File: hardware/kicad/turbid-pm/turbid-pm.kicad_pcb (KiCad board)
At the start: 2 copper layers, 10 parts, among them J1 Pi connection, J2 PMS 7003, J3 Turbidity

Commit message: added 3d print source
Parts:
- removed D2: Turbidity Ok LED, LED_THT:LED_D3.0mm_Clear
- added J4: Temp sensor A, Connector_PinSocket_2.54mm:PinSocket_1x03_P2.54mm_Vertical, F.Cu at (94.0, 81.3)
- added J5: Temp sensor B, Connector_PinSocket_2.54mm:PinSocket_1x03_P2.54mm_Vertical, F.Cu at (102.9, 81.3)
- added R5: 4.7K, Resistor_THT:R_Axial_DIN0207_L6.3mm_D2.5mm_P10.16mm_Horizontal, F.Cu at (100.3, 68.6)
- J1: value Pi connection -> Raspbery Pi
- J3: value Turbidity -> Turbidity sensor
- R1: value R -> 1K
- R2: value R -> 10K
- R4: value R -> 4.7K
- moved R4 5.24 mm to (97.8, 68.6), turned to 270 degrees
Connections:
- net /rx renamed /RX
- net /scl renamed /SCL
- net /sda renamed /SDA
- net /tx renamed /TX
- A1 pad 8: (no net) -> Net-(A1-Pad8)
- R4 pad 2: Net-(D2-Pad2) -> +5V
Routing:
- net +5V: track 77.3 -> 116.2 mm, vias 5 -> 8
- net Net-(A1-Pad7): track 10.2 -> 35.6 mm, vias 0 -> 3
- net Net-(A1-Pad8): track 0.00 -> 14.5 mm, vias 0 -> 2
- net Net-(D2-Pad2): track 12.7 -> 0.00 mm
- net Earth: track 180.3 -> 186.7 mm
- net Net-(A1-Pad5): track 33.6 -> 34.9 mm, vias 2 -> 3

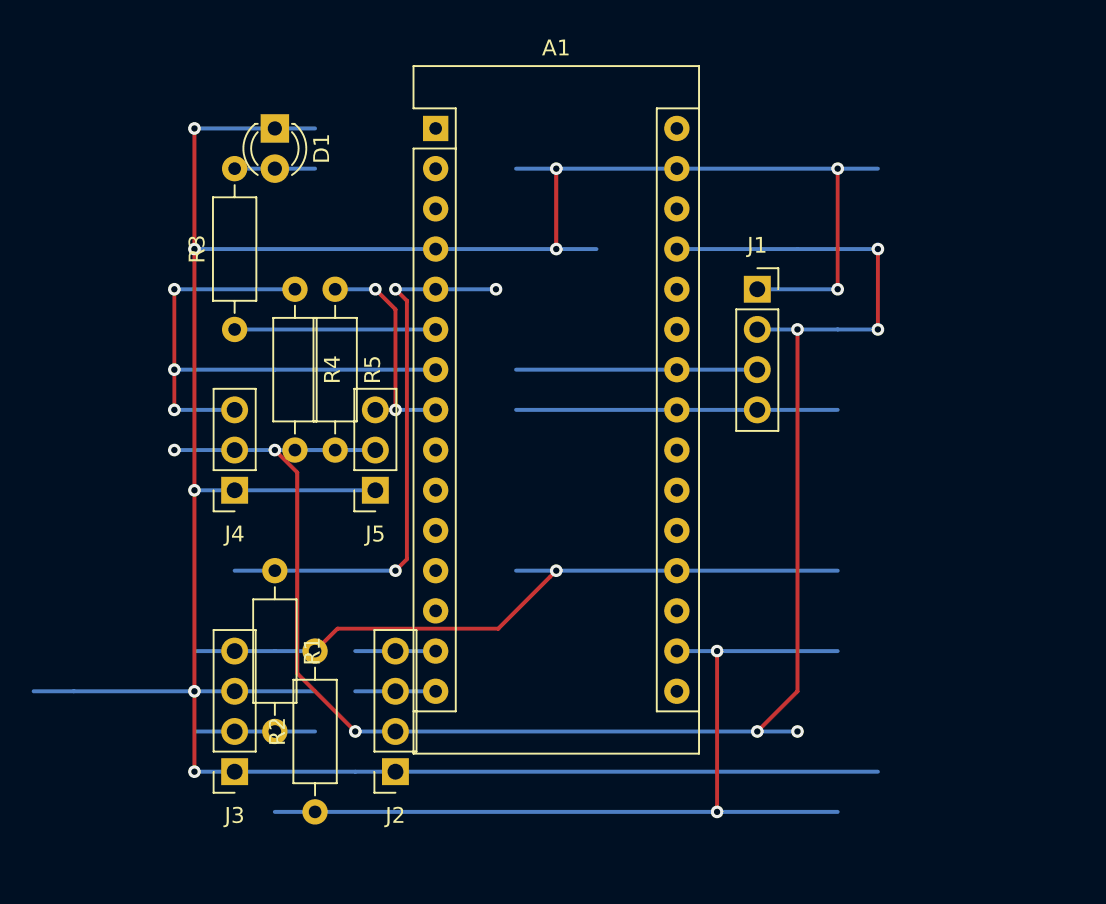
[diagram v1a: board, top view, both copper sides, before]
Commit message: new firmware and docs
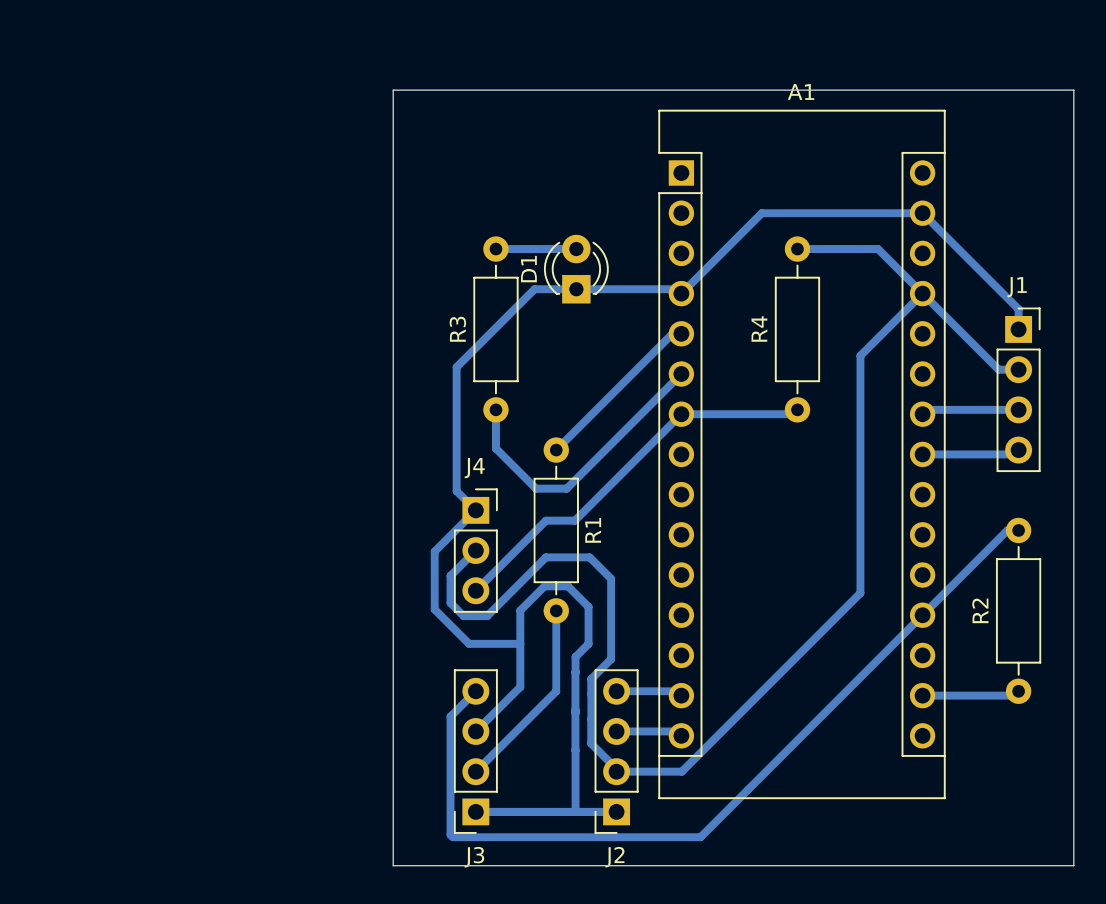
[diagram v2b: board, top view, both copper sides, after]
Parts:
- removed J5: Temp sensor B, Connector_PinSocket_2.54mm:PinSocket_1x03_P2.54mm_Vertical
- removed R5: 4.7K, Resistor_THT:R_Axial_DIN0207_L6.3mm_D2.5mm_P10.16mm_Horizontal
- J4: value Temp sensor A -> Temp sensor
- moved R2 45.1 mm to (143.5, 94.0)
- moved R4 32.7 mm to (129.5, 76.2), turned to 90 degrees
- moved D1 21.6 mm to (115.6, 68.6), turned to 90 degrees
- moved R1 19.3 mm to (114.3, 78.7)
- moved R3 17.3 mm to (110.5, 76.2)
- moved J1 16.7 mm to (143.5, 71.1)
- moved A1 15.8 mm to (122.2, 61.2)
- moved J3 15.5 mm to (109.2, 101.6)
- moved J4 15.3 mm to (109.2, 82.5), turned to 0 degrees
- moved J2 14.2 mm to (118.1, 101.6)
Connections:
- A1 pad 8: Net-(A1-Pad8) -> (no net)
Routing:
- net Earth: track 186.7 -> 112.2 mm, vias 9 -> 0
- net +3V3: track 55.9 -> 6.18 mm, vias 2 -> 0
- net +5V: track 116.2 -> 87.7 mm, vias 8 -> 0
- net Net-(A1-Pad5): track 34.9 -> 10.9 mm, vias 3 -> 0
- net Net-(A1-Pad8): track 14.5 -> 0.00 mm, vias 2 -> 0
- net /SDA: track 20.3 -> 6.18 mm
- net Net-(A1-Pad7): track 35.6 -> 25.1 mm, vias 3 -> 0
- net /SCL: track 15.2 -> 6.18 mm
- net Net-(A1-Pad19): track 45.3 -> 53.7 mm, vias 2 -> 0
- net Net-(A1-Pad6): track 12.7 -> 18.2 mm
- net Net-(J3-Pad2): track 7.62 -> 12.3 mm
- net /RX: track 5.08 -> 4.21 mm
- net /TX: track 5.08 -> 4.21 mm
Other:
- board outline added: 43 x 49 mm
- net class Default: clearance 0.2 -> 0.5; trace_width 0.25 -> 0.5
- rule trace_clearance: 0.2 -> 0.5

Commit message: adding final action bits
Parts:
- added C1: C, Capacitor_THT:C_Axial_L5.1mm_D3.1mm_P7.50mm_Horizontal, F.Cu at (140.5, 73.5)
- added C2: C, Capacitor_THT:C_Axial_L5.1mm_D3.1mm_P7.50mm_Horizontal, F.Cu at (106.5, 87.5)
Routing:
- net Earth: track 112.2 -> 117.9 mm
- net +5V: track 87.7 -> 92.3 mm
- added copper zone on B.Cu, net Earth
